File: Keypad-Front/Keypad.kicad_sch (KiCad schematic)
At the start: 55 parts, among them J1 RTC STEMMA QT, J10 EXP QWIIC, J11 TOUCH QWIIC, J2 LED BOARD 1, J3 LED BOARD 2, J4 LED BOARD 3, J5 LED BOARD 4, J6 Conn_01x06, J7 Conn_01x06, J8 Feedback, J9 Conn_01x08, U1 DS3231MZ, U2 LM1117-3.3, U3 CAP1214

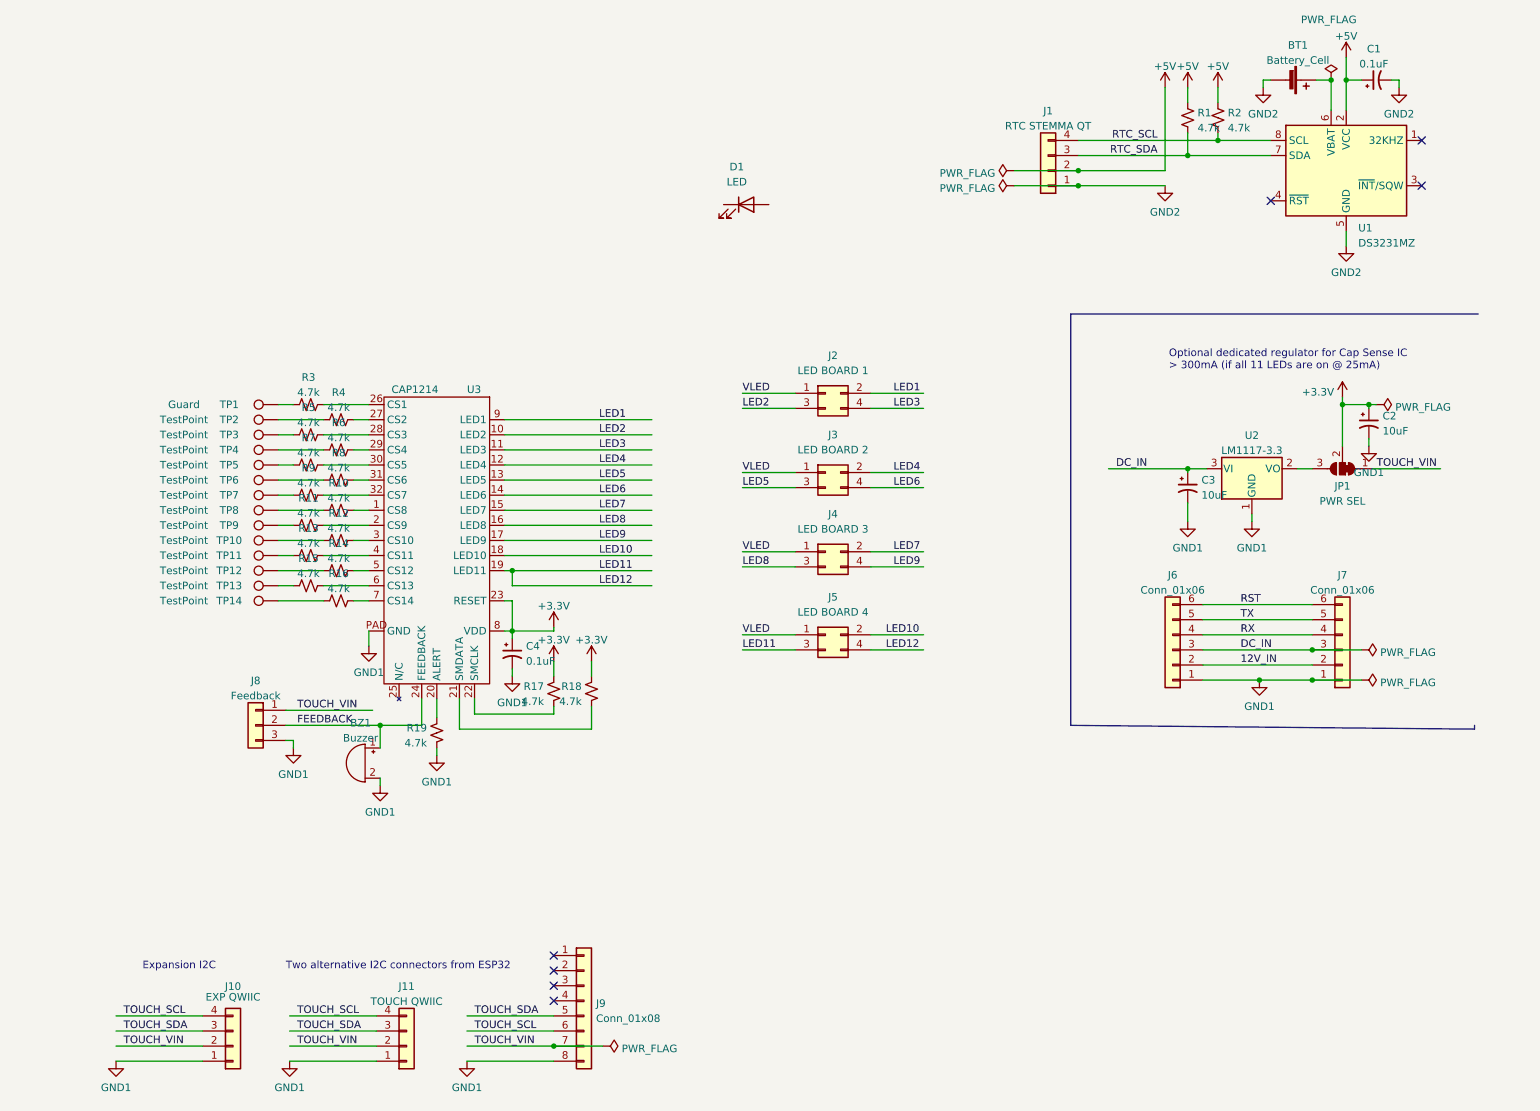
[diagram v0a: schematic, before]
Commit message: Back to a one-board design with rear-firing LEDs
Giving up on the UV LED idea for now.
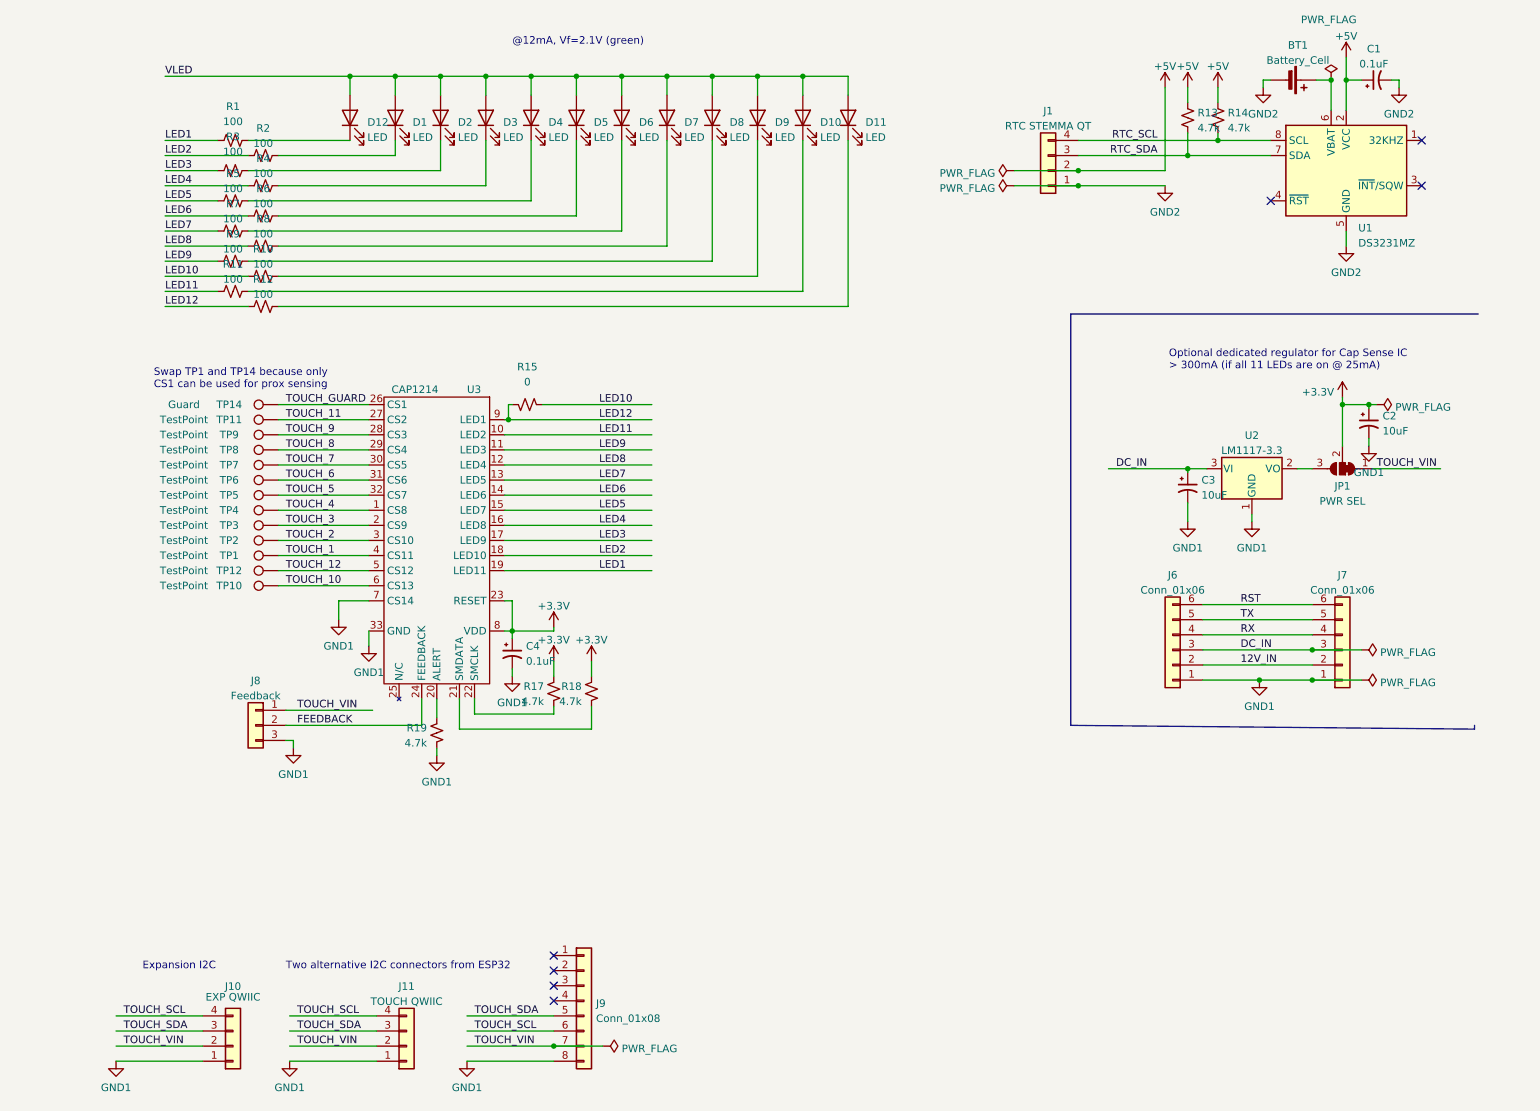
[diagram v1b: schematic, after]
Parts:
- removed BZ1: Buzzer, symbol Device:Buzzer
- removed J2: LED BOARD 1, Connector_PinHeader_2.54mm:PinHeader_2x02_P2.54mm_Vertical_SMD, symbol Connector_Generic:Conn_02x02_Odd_Even
- removed J3: LED BOARD 2, Connector_PinHeader_2.54mm:PinHeader_2x02_P2.54mm_Vertical_SMD, symbol Connector_Generic:Conn_02x02_Odd_Even
- removed J4: LED BOARD 3, Connector_PinHeader_2.54mm:PinHeader_2x02_P2.54mm_Vertical_SMD, symbol Connector_Generic:Conn_02x02_Odd_Even
- removed J5: LED BOARD 4, Connector_PinHeader_2.54mm:PinHeader_2x02_P2.54mm_Vertical_SMD, symbol Connector_Generic:Conn_02x02_Odd_Even
- removed R13, R14: 4.7k, Resistor_SMD:R_0805_2012Metric_Pad1.20x1.40mm_HandSolder, symbol Device:R_Small_US
- removed TP13: TestPoint, symbol Connector:TestPoint
- added D10, D11, D12, D2, D3, D4, D5, D6, D7, D8, D9: LED, Keypad:SunLED_3.2x2.8mm_ReverseMount, symbol Device:LED
- added R15: 0, Resistor_SMD:R_0805_2012Metric_Pad1.20x1.40mm_HandSolder, symbol Device:R_Small_US
- BT1: footprint (none) -> Battery:BatteryHolder_MPD_BC2003_1x2032
- J1: footprint (none) -> Transflective:JST-SH-4-VERT-SMD
- R1: renamed from R15; value 4.7k -> 100
- R10, R11, R12, R3, R4, R5, R6, R7, R8, R9: value 4.7k -> 100
- R2: renamed from R16; value 4.7k -> 100
- TP1: renamed from TP14; footprint (none) -> Keypad:Touch_Pad_D1.0mm
- TP10, TP11, TP12, TP2, TP3, TP4, TP5, TP6, TP7, TP8, TP9: footprint (none) -> Keypad:Touch_Pad_D1.0mm
- TP14: renamed from TP1; footprint Capacitor_SMD:C_0805_2012Metric_Pad1.18x1.45mm_HandSolder -> Keypad:Touch_Pad_D1.0mm
- U3: footprint (none) -> Package_DFN_QFN:QFN-32-1EP_5x5mm_P0.5mm_EP3.3x3.3mm_ThermalVias
- renumbered R1 to R13, R2 to R14
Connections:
- net GND1: now also U3.33 (GND), U3.7 (CS14); no longer U3.PAD (GND)
- net LED1: now also R1.1, U3.19 (LED11); no longer U3.9 (LED1)
- net LED10: now also R10.1, R15.2; no longer U3.18 (LED10)
- net LED11: now also R11.1, U3.10 (LED2); no longer U3.19 (LED11)
- net LED2: now also R2.1, U3.18 (LED10); no longer U3.10 (LED2)
- net LED3: now also R3.1, U3.17 (LED9); no longer U3.11 (LED3)
- net LED4: now also R4.1, U3.16 (LED8); no longer U3.12 (LED4)
- net LED5: now also R5.1, U3.15 (LED7); no longer U3.13 (LED5)
- net LED6: now also R6.1
- net LED7: now also R7.1, U3.13 (LED5); no longer U3.15 (LED7)
- net LED8: now also R8.1, U3.12 (LED4); no longer U3.16 (LED8)
- net LED9: now also R9.1, U3.11 (LED3); no longer U3.17 (LED9)
- net VLED: now also D1.2 (A), D10.2 (A), D11.2 (A), D12.2 (A), D2.2 (A), D3.2 (A), D4.2 (A), D5.2 (A), D6.2 (A), D7.2 (A), D8.2 (A), D9.2 (A)
- net at D1.1 (K): now also R2.2
- net TOUCH_5: now reaches TP5.1
- net TOUCH_5: now also U3.32 (CS7); no longer R7.1
- net at R7.2: now also D6.1 (K); no longer U3.30 (CS5)
- net TOUCH_2: now reaches TP2.1
- net TOUCH_2: now also U3.3 (CS10); no longer R4.1
- net at R4.2: now also D3.1 (K); no longer U3.27 (CS2)
- net LED12: now reaches R12.1
- net LED12: now also U3.9 (LED1), R15.1; no longer TP10.1
- net TOUCH_6: now reaches TP6.1
- net TOUCH_6: now also U3.31 (CS6); no longer R8.1
- net at R8.2: now also D7.1 (K); no longer U3.31 (CS6)
- net TOUCH_3: now reaches TP3.1
- net TOUCH_3: now also U3.2 (CS9); no longer R5.1
- net at R12.2: now also D11.1 (K); no longer U3.3 (CS10)
- net TOUCH_12: now reaches TP12.1
- net TOUCH_12: now also U3.5 (CS12)
- net TOUCH_GUARD: now reaches TP14.1
- net TOUCH_GUARD: now also U3.26 (CS1); no longer R3.1
- net at R5.2: now also D4.1 (K); no longer U3.28 (CS3)
- net TOUCH_8: now reaches TP8.1
- net TOUCH_8: now also U3.29 (CS4); no longer R10.1
- net at R10.2: now also D9.1 (K); no longer U3.1 (CS8)
- net TOUCH_4: now reaches TP4.1
- net TOUCH_4: now also U3.1 (CS8); no longer R6.1
- net at R6.2: now also D5.1 (K); no longer U3.29 (CS4)
- net TOUCH_7: now reaches TP7.1
- net TOUCH_7: now also U3.30 (CS5); no longer R9.1
- net at R9.2: now also D8.1 (K); no longer U3.32 (CS7)
- net at R11.2: now also D10.1 (K); no longer U3.2 (CS9)
- net at R3.2: now also D2.1 (K); no longer U3.26 (CS1)
- net TOUCH_1: now reaches U3.4 (CS11)
- net TOUCH_1: now also TP1.1
- net at R1.2: now also D12.1 (K); no longer U3.6 (CS13)
- net TOUCH_11: now reaches TP11.1
- net TOUCH_11: now also U3.27 (CS2)
- net TOUCH_9: now reaches TP9.1
- net TOUCH_9: now also U3.28 (CS3); no longer R11.1
- new net TOUCH_10: TP10.1, U3.6 (CS13)
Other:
- note added: "@12mA, Vf=2.1V (green)"
- note added: "Swap TP1 and TP14 because only CS1 can be used for prox sensing"
- moved on the sheet: R1, R10, R11, R12, R2, R3, R4, R5, R6, R7, R8, R9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

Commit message: Steady work on Keypad PCB
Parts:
- added JP2: PWR SEL, Jumper:SolderJumper-3_P1.3mm_Bridged12_RoundedPad1.0x1.5mm, symbol Jumper:SolderJumper_3_Bridged12
- J10, J11: footprint (none) -> Transflective:JST-SH-4-VERT-SMD
- J6: value Conn_01x06 -> JST-PH 6; footprint Connector_JST:JST_PH_S6B-PH-K_1x06_P2.00mm_Horizontal -> Keypad:JST-PH-6-SMD
- J7: value Conn_01x06 -> JST-PH 6; footprint (none) -> Keypad:JST-PH-6-SMD
- J9: value Conn_01x08 -> JST-PH 8; now left out of the parts list
- U2: footprint (none) -> Package_TO_SOT_SMD:SOT-223-3_TabPin2
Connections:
- net +3.3V: now also JP2.2 (C)
- net DC_IN: now also JP2.3 (B)
- net VLED renamed LED_VIN
- net LED_VIN: now also JP2.1 (A)
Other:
- note added: "(+5V)"
- note added: "Interposer"
- note added: "Optional dedicated regulator for Cap Sense IC > 150mA (if all 12 LEDs are on @ 12mA)"
- note added: "Optional higher-voltage supply for white/blue LEDs"
- note added: "Two alternative I2C connectors from ESP32 (but we're only going to use the QWIIC one; we'll make a JST-PH-8 to QWIIC cable to handle the other case)"
- note removed: "Optional dedicated regulator for Cap Sense IC > 300mA (if all 11 LEDs are on @ 25mA)"
- note removed: "Two alternative I2C connectors from ESP32"
- moved on the sheet: J6, J7

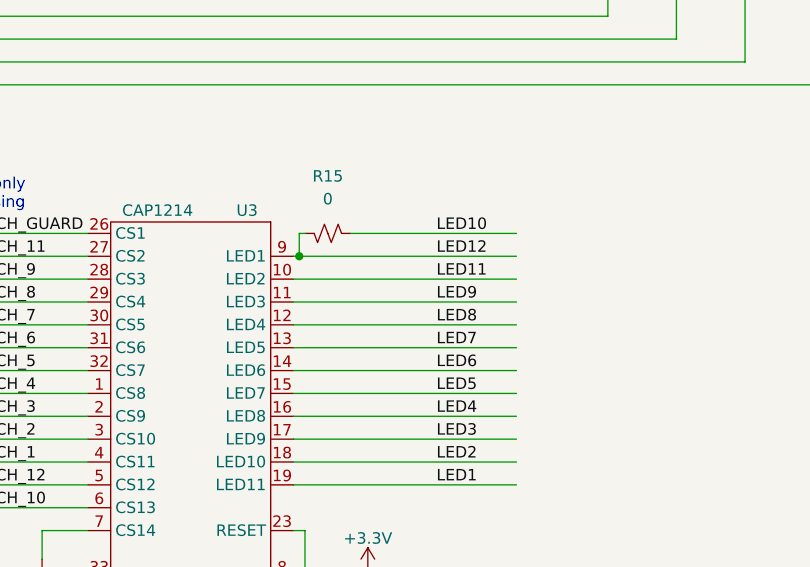
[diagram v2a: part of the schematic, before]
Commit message: Attempt 2 at routing, cap sensor at bottom
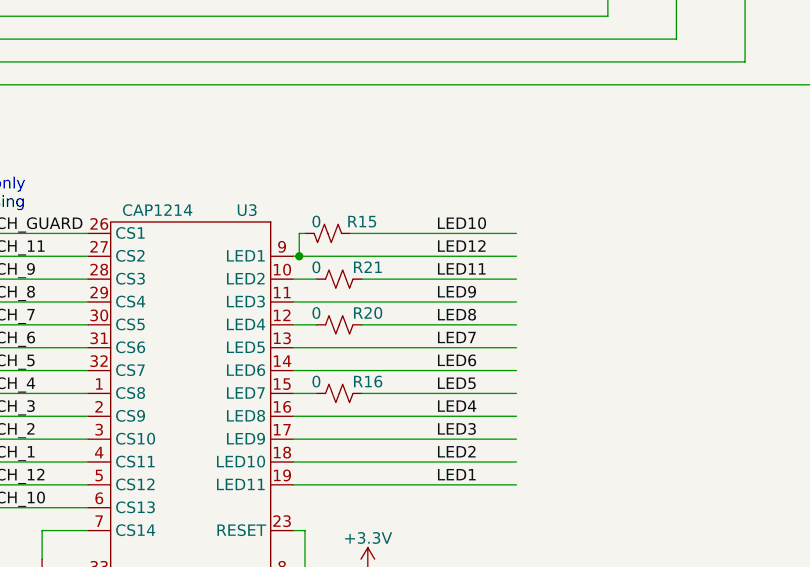
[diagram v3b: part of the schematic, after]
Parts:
- added R16, R20, R21: 0, Resistor_SMD:R_1206_3216Metric_Pad1.30x1.75mm_HandSolder, symbol Device:R_Small_US
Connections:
- net LED11: now also R21.1; no longer U3.10 (LED2)
- net LED5: now also R16.1; no longer U3.15 (LED7)
- net LED8: now also R20.1; no longer U3.12 (LED4)
- new net: R20.2, U3.12 (LED4)
- new net: R16.2, U3.15 (LED7)
- new net: R21.2, U3.10 (LED2)
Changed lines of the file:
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@@
     (stroke (width 0) (type default))
   )
+  (wire (pts (xy 108.585 85.725) (xy 125.73 85.725))
+    (stroke (width 0) (type default))
+  )
   (wire (pts (xy 125.73 80.645) (xy 107.315 80.645))
     (stroke (width 0) (type default))
@@
     (stroke (width 0) (type default))
   )
-  (wire (pts (xy 100.965 85.725) (xy 125.73 85.725))
-    (stroke (width 0) (type default))
-  )
   (wire (pts (xy 105.41 25.4) (xy 105.41 28.575))
     (stroke (width 0) (type default))
@@
     (stroke (width 0) (type default))
   )
-  (wire (pts (xy 100.965 98.425) (xy 125.73 98.425))
-    (stroke (width 0) (type default))
-  )
   (wire (pts (xy 43.815 43.815) (xy 57.785 43.815))
     (stroke (width 0) (type default))
@@
     (stroke (width 0) (type default))
   )
+  (wire (pts (xy 100.965 85.725) (xy 103.505 85.725))
+    (stroke (width 0) (type default))
+  )
   (wire (pts (xy 90.17 25.4) (xy 90.17 28.575))
     (stroke (width 0) (type default))
@@
     (stroke (width 0) (type default))
   )
+  (wire (pts (xy 108.585 90.805) (xy 125.73 90.805))
+    (stroke (width 0) (type default))
+  )
   (wire (pts (xy 64.135 132.08) (xy 78.74 132.08))
     (stroke (width 0) (type default))
   )
+  (wire (pts (xy 100.965 98.425) (xy 103.505 98.425))
+    (stroke (width 0) (type default))
+  )
   (wire (pts (xy 64.135 134.62) (xy 86.995 134.62))
     (stroke (width 0) (type default))
@@
     (stroke (width 0) (type default))
   )
+  (wire (pts (xy 108.585 98.425) (xy 125.73 98.425))
+    (stroke (width 0) (type default))
+  )
   (wire (pts (xy 109.22 188.595) (xy 117.475 188.595))
     (stroke (width 0) (type default))
@@
     (stroke (width 0) (type default))
   )
+  (wire (pts (xy 100.965 90.805) (xy 103.505 90.805))
+    (stroke (width 0) (type default))
+  )
   (wire (pts (xy 143.51 59.055) (xy 143.51 36.195))
     (stroke (width 0) (type default))
@@
     (stroke (width 0) (type default))
   )
-  (wire (pts (xy 100.965 90.805) (xy 125.73 90.805))
-    (stroke (width 0) (type default))
-  )
   (wire (pts (xy 93.345 135.255) (xy 115.57 135.255))
     (stroke (width 0) (type default))
@@
   )
   (symbol (lib_id "Device:R_Small_US") (at 104.775 80.645 90) (mirror x) (unit 1)
-    (in_bom yes) (on_board yes) (dnp no) (fields_autoplaced)
-    (property "Reference" "R15" (at 104.775 74.295 90)
+    (in_bom yes) (on_board yes) (dnp no)
+    (property "Reference" "R15" (at 108.585 79.375 90)
       (effects (font (size 1.27 1.27)))
     )
-    (property "Value" "0" (at 104.775 76.835 90)
+    (property "Value" "0" (at 103.505 79.375 90)
       (effects (font (size 1.27 1.27)))
     )
@@
     )
   )
+  (symbol (lib_id "Device:R_Small_US") (at 106.045 90.805 270) (unit 1)
+    (in_bom yes) (on_board yes) (dnp no)
+    (property "Reference" "R20" (at 109.22 89.535 90)
+      (effects (font (size 1.27 1.27)))
+    )
+    (property "Value" "0" (at 103.505 89.535 90)
+      (effects (font (size 1.27 1.27)))
+    )
+    (property "Footprint" "Resistor_SMD:R_1206_3216Metric_Pad1.30x1.75mm_HandSolder" (at 106.045 90.805 0)
+      (effects (font (size 1.27 1.27)) hide)
+    )
+    (property "Datasheet" "~" (at 106.045 90.805 0)
+      (effects (font (size 1.27 1.27)) hide)
+    )
+    (pin "1")
+    (pin "2")
+    (instances
+      (project "Keypad"
+        (path "/ed47ce54-8b56-4a78-a942-9443bc7041ac"
+          (reference "R20") (unit 1)
+        )
+      )
+    )
+  )
+  (symbol (lib_id "Device:R_Small_US") (at 106.045 98.425 270) (unit 1)
+    (in_bom yes) (on_board yes) (dnp no)
+    (property "Reference" "R16" (at 109.22 97.155 90)
+      (effects (font (size 1.27 1.27)))
+    )
+    (property "Value" "0" (at 103.505 97.155 90)
+      (effects (font (size 1.27 1.27)))
+    )
+    (property "Footprint" "Resistor_SMD:R_1206_3216Metric_Pad1.30x1.75mm_HandSolder" (at 106.045 98.425 0)
+      (effects (font (size 1.27 1.27)) hide)
+    )
+    (property "Datasheet" "~" (at 106.045 98.425 0)
+      (effects (font (size 1.27 1.27)) hide)
+    )
+    (pin "1")
+    (pin "2")
+    (instances
+      (project "Keypad"
+        (path "/ed47ce54-8b56-4a78-a942-9443bc7041ac"
+          (reference "R16") (unit 1)
+        )
+      )
+    )
+  )
   (symbol (lib_id "Keypad:CAP1214") (at 84.455 97.155 270) (unit 1)
     (in_bom yes) (on_board yes) (dnp no)
@@
         )
       )
+    )
+  )
+  (symbol (lib_id "Device:R_Small_US") (at 106.045 85.725 270) (unit 1)
+    (in_bom yes) (on_board yes) (dnp no)
+    (property "Reference" "R21" (at 109.22 84.455 90)
+      (effects (font (size 1.27 1.27)))
+    )
+    (property "Value" "0" (at 103.505 84.455 90)
+      (effects (font (size 1.27 1.27)))
+    )
+    (property "Footprint" "Resistor_SMD:R_1206_3216Metric_Pad1.30x1.75mm_HandSolder" (at 106.045 85.725 0)
+      (effects (font (size 1.27 1.27)) hide)
+    )
+    (property "Datasheet" "~" (at 106.045 85.725 0)
+      (effects (font (size 1.27 1.27)) hide)
+    )
+    (pin "1")
+    (pin "2")
+    (instances
+      (project "Keypad"
+        (path "/ed47ce54-8b56-4a78-a942-9443bc7041ac"
+          (reference "R21") (unit 1)
+        )
+      )
